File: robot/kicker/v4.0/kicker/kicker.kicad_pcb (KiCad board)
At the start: 6 copper layers, 172.6 x 120 mm, 190 parts, among them J1 JST-SM10B-GHS, J11 JST-SM10B-GHS, J2 BM04B-PASS-1-TFT, J3 XT30-F, J4 Conn_ARM_JTAG_SWD_10, J5 2165711002, J6 2165711002, J7 SM12B-ZESS-TB, J8 SM08B-GHS-TB, J9 SM08B-GHS-TB, Q1 BSS138K, Q2 BSS138K, Q3 IXGA48N60A3, Q4 IXGA48N60A3, Q5 BSC0402NSATMA1, SW1 BTN0, SW2 SW_DIP_x04, SW3 RST, U1 TLV70030_SOT353, U2 TPS7B86, U3 STM32G474VETx, U4 SK9822, U5 AT25DF041x-UxN-x, U6 SK9822, U7 IX4427, U8 LT3757EMSE, Y1 Q13FC13500005, Y2 TAXM8M4RDBCCT2T

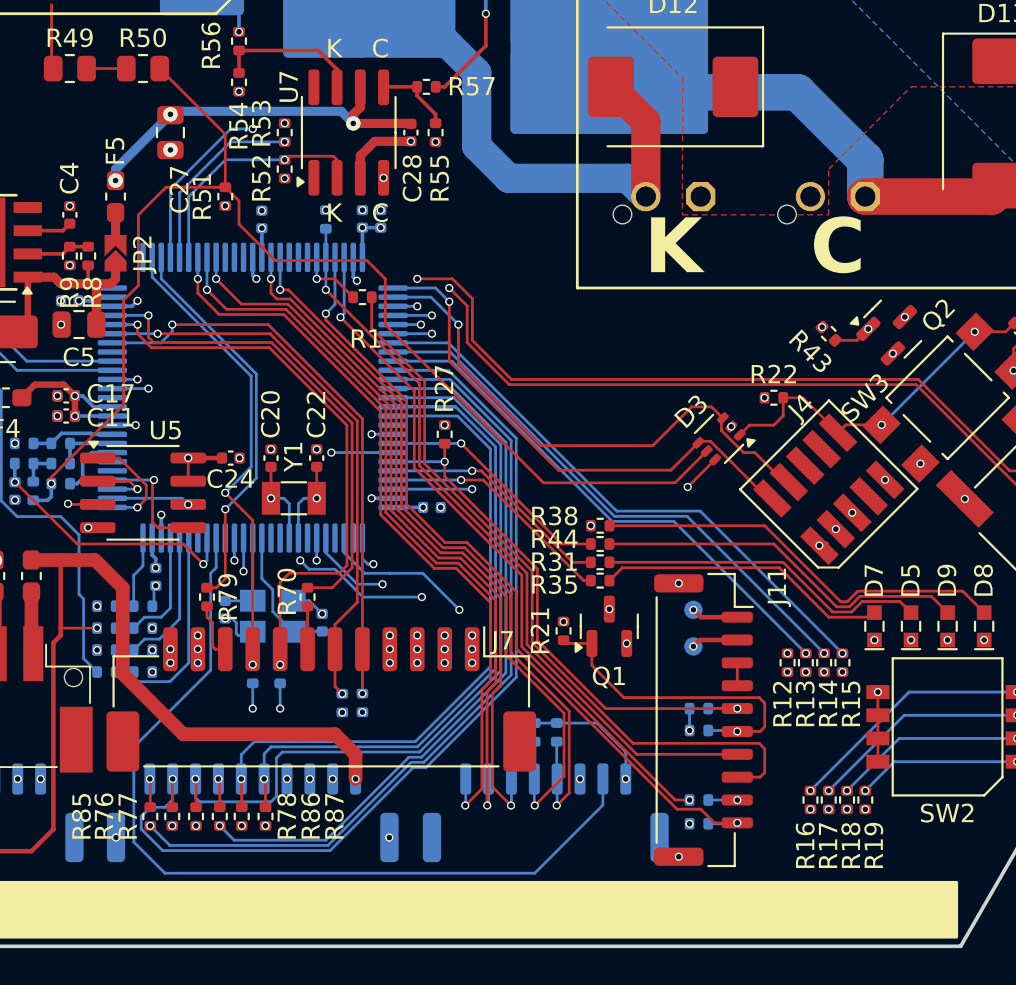
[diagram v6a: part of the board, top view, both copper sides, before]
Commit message: fixed to kicker v4
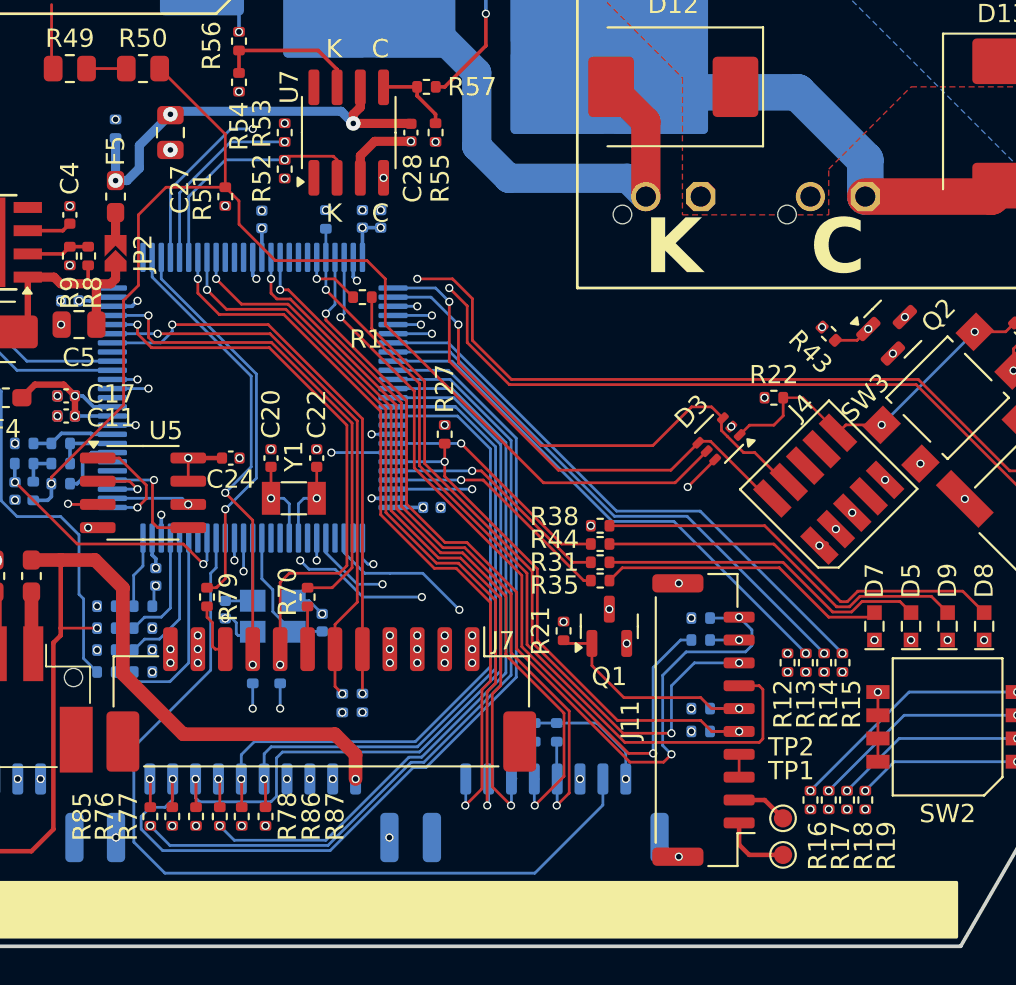
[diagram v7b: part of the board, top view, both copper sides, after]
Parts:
- added R88: 0, Resistor_SMD:R_0402_1005Metric, B.Cu at (202.5, 140.3)
- J11: value JST-SM10B-GHS -> JST-BM10B-GHS; footprint Connector_JST:JST_GH_SM10B-GHS-TB_1x10-1MP_P1.25mm_Horizontal -> Connector_JST:JST_GH_BM10B-GHS-TBT_1x10-1MP_P1.25mm_Vertical
- J3: value XT30-F -> XT30-M
- TP1, TP2: moved to F.Cu
- moved TP1 14.3 mm to (239.0, 180.0), turned to -45 degrees
- moved R82 11.3 mm to (234.5, 167.1)
- moved TP2 10.6 mm to (239.0, 178.0), turned to -45 degrees
- moved R2 8.75 mm to (234.5, 168.2)
- moved R83 1.25 mm to (234.5, 173.2)
- moved R84 1.20 mm to (234.5, 172.0)
- turned J11 to 90 degrees
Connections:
- C39 pad 1: +VSW -> Net-(U8-INTVCC)
- U8 pad 8: +VSW -> Net-(U8-INTVCC)
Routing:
- net +VSW: track 117.8 -> 49.3 mm, vias 5 -> 4
- net Net-(U8-INTVCC): track 0.00 -> 67.9 mm, vias 0 -> 2
- net /COMS.CTS: track 44.3 -> 51.4 mm, vias 2 -> 3
- net /COMS.RX: track 41.3 -> 46.6 mm
- net /COMS.RTS: track 38.1 -> 42.5 mm
- net /COMS.RST: track 17.6 -> 13.5 mm
- net Net-(J11-Pin_8): track 40.5 -> 39.0 mm, vias 0 -> 2
- net /5v0_UPSTREAM: track 2.57 -> 3.83 mm, vias 1 -> 0
- net GND: track 127.7 -> 126.7 mm, vias 211 -> 212
- net /COMS.BOOT0: track 29.8 -> 30.4 mm
- net /3v3_UPSTREAM: track 2.54 -> 2.81 mm, vias 1 -> 0
